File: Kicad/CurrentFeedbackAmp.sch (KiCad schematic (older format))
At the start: 123 parts, among them J1 Test_Etapa_3_Inf, J10 Protecc_Sup_In1, J11 Protecc_Inf_In1, J12 Protecc_Sup_In2, J13 Test_Etapa_3_Inf, J14 Entrada, J15 Salida masa2, J16 Salida tierra, J17 Salida senal, J2 Test_Realim_Out, J3 Salida masa1, J4 Protecc_Sup_Out, J5 Protecc_Inf_Out, J6 Conector Vcc, J7 Conector Vdd, J8 Test_Etapa_3_Inf, J9 Test_Etapa_3_Sup, Q1 TIP42C, Q10 BC559, Q11 BC549, Q12 BC559, Q13 BC559, Q14 BC559, Q15 BC559, Q16 BC549, Q17 BC549, Q18 BC549, Q19 BC559, Q2 BD135, Q20 BC549, Q21 BC559, Q22 BC549, Q23 BC549, Q24 BD136, Q25 BC559, Q26 BC549, Q27 BC549, Q28 BC549, Q29 BC559, Q3 BD136, Q30 BC559, Q31 BC549, Q32 BC559, Q33 BD135, Q34 TIP41C, Q35 BC858, Q36 BC848, Q37 BC848, Q38 BC848, Q4 BC549, Q40 BC858, Q41 BC858, Q5 BC549, Q6 BC559, Q7 BC559, Q8 BC549, Q9 BC559, U1 LM7812_TO220, U2 TL082, U3 LM7912_TO220, U4 LM7805_TO220, U5 LM7905_TO220

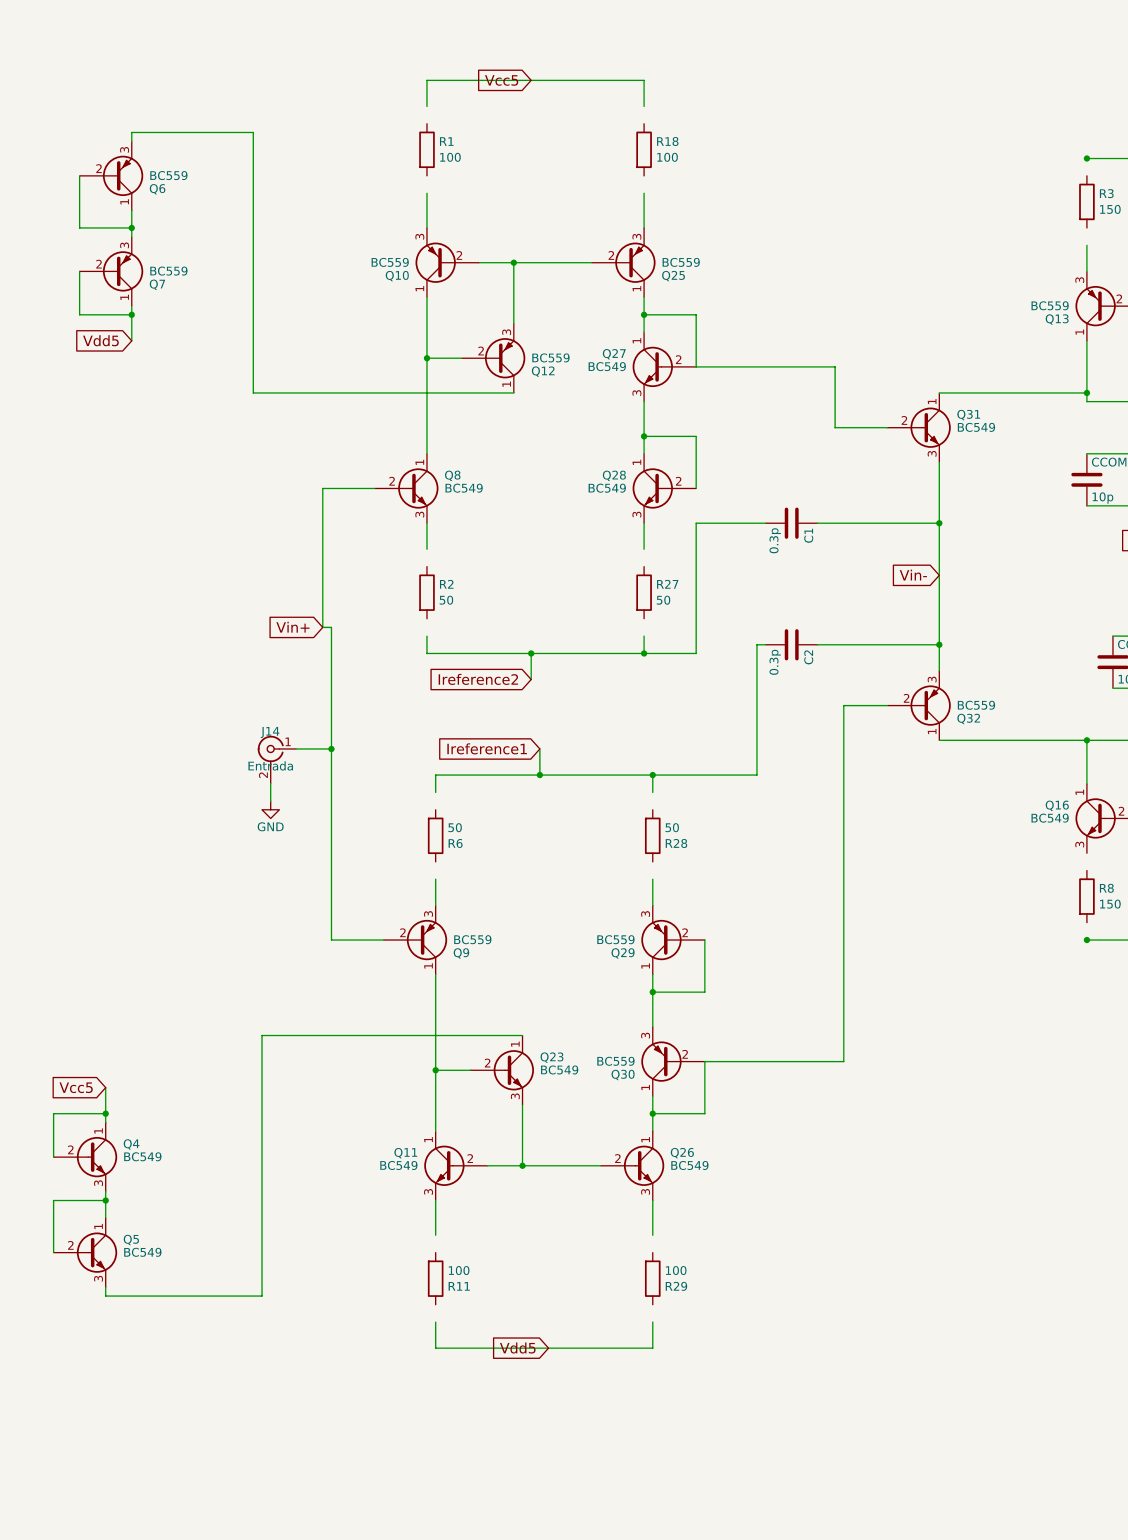
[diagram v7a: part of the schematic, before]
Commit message: Cambios en transitores de etapa siguiente a la fuente de corriente por SMD
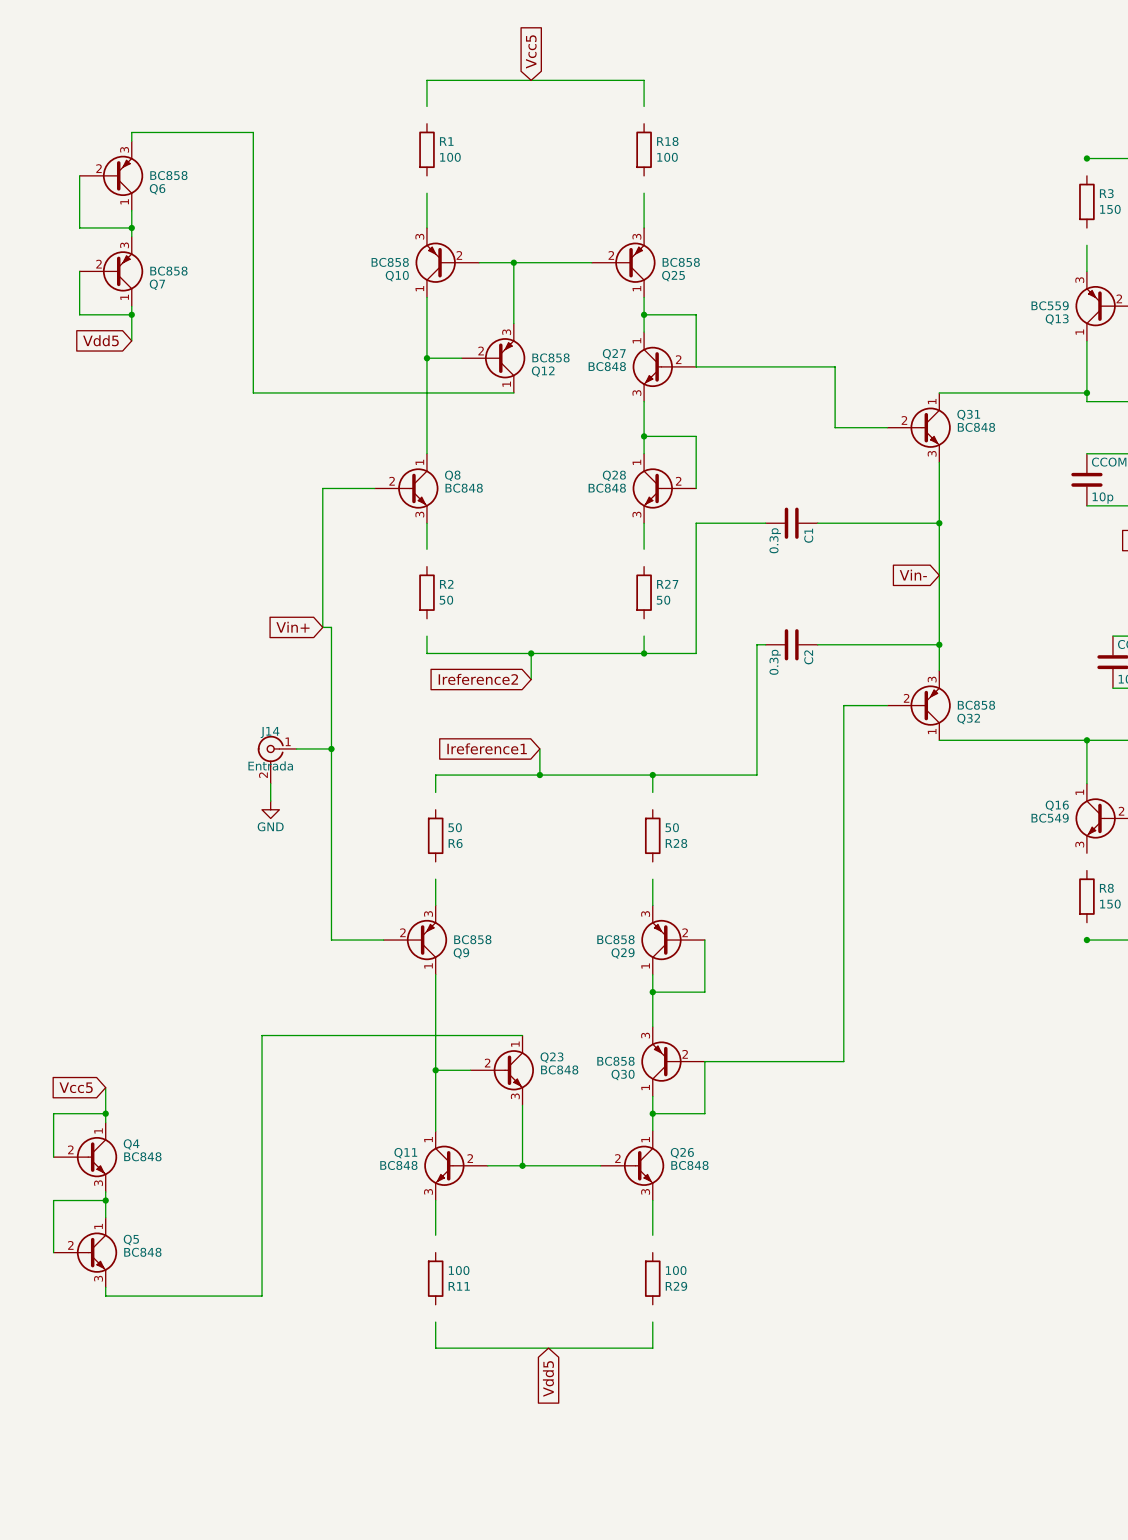
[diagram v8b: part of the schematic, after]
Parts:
- Q10, Q12, Q25, Q29, Q30, Q32, Q6, Q7, Q9: value BC559 -> BC858
- Q11, Q23, Q26, Q27, Q28, Q31, Q4, Q5, Q8: value BC549 -> BC848
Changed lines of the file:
@@
 P 10450 1850
 F 0 "Q10" H 10650 1925 50  0000 L CNN
-F 1 "BC559" H 10650 1850 50  0000 L CNN
+F 1 "BC858" H 10650 1850 50  0000 L CNN
 F 2 "TO_SOT_Packages_THT:TO-92_Inline_Narrow_Oval" H 10650 1775 50  0001 L CIN
 F 3 "" H 10450 1850 50  0001 L CNN
@@
 P 11500 1850
 F 0 "Q25" H 11700 1925 50  0000 L CNN
-F 1 "BC559" H 11700 1850 50  0000 L CNN
+F 1 "BC858" H 11700 1850 50  0000 L CNN
 F 2 "TO_SOT_Packages_THT:TO-92_Inline_Narrow_Oval" H 11700 1775 50  0001 L CIN
 F 3 "" H 11500 1850 50  0001 L CNN
@@
 P 10750 2400
 F 0 "Q12" H 10950 2475 50  0000 L CNN
-F 1 "BC559" H 10950 2400 50  0000 L CNN
+F 1 "BC858" H 10950 2400 50  0000 L CNN
 F 2 "TO_SOT_Packages_THT:TO-92_Inline_Narrow_Oval" H 10950 2325 50  0001 L CIN
 F 3 "" H 10750 2400 50  0001 L CNN
@@
 P 8550 1350
 F 0 "Q6" H 8750 1425 50  0000 L CNN
-F 1 "BC559" H 8750 1350 50  0000 L CNN
+F 1 "BC858" H 8750 1350 50  0000 L CNN
 F 2 "TO_SOT_Packages_THT:TO-92_Inline_Narrow_Oval" H 8750 1275 50  0001 L CIN
 F 3 "" H 8550 1350 50  0001 L CNN
@@
 P 8550 1900
 F 0 "Q7" H 8750 1975 50  0000 L CNN
-F 1 "BC559" H 8750 1900 50  0000 L CNN
+F 1 "BC858" H 8750 1900 50  0000 L CNN
 F 2 "TO_SOT_Packages_THT:TO-92_Inline_Narrow_Oval" H 8750 1825 50  0001 L CIN
 F 3 "" H 8550 1900 50  0001 L CNN
@@
 P 11700 2450
 F 0 "Q27" H 11900 2525 50  0000 L CNN
-F 1 "BC549" H 11900 2450 50  0000 L CNN
+F 1 "BC848" H 11900 2450 50  0000 L CNN
 F 2 "TO_SOT_Packages_THT:TO-92_Inline_Narrow_Oval" H 11900 2375 50  0001 L CIN
 F 3 "" H 11700 2450 50  0001 L CNN
@@
 P 11700 3150
 F 0 "Q28" H 11900 3225 50  0000 L CNN
-F 1 "BC549" H 11900 3150 50  0000 L CNN
+F 1 "BC848" H 11900 3150 50  0000 L CNN
 F 2 "TO_SOT_Packages_THT:TO-92_Inline_Narrow_Oval" H 11900 3075 50  0001 L CIN
 F 3 "" H 11700 3150 50  0001 L CNN
@@
 P 10250 3150
 F 0 "Q8" H 10450 3225 50  0000 L CNN
-F 1 "BC549" H 10450 3150 50  0000 L CNN
+F 1 "BC848" H 10450 3150 50  0000 L CNN
 F 2 "TO_SOT_Packages_THT:TO-92_Inline_Narrow_Oval" H 10450 3075 50  0001 L CIN
 F 3 "" H 10250 3150 50  0001 L CNN
@@
 P 13200 2800
 F 0 "Q31" H 13400 2875 50  0000 L CNN
-F 1 "BC549" H 13400 2800 50  0000 L CNN
+F 1 "BC848" H 13400 2800 50  0000 L CNN
 F 2 "TO_SOT_Packages_THT:TO-92_Inline_Narrow_Oval" H 13400 2725 50  0001 L CIN
 F 3 "" H 13200 2800 50  0001 L CNN
@@
 P 10300 5750
 F 0 "Q9" H 10500 5825 50  0000 L CNN
-F 1 "BC559" H 10500 5750 50  0000 L CNN
+F 1 "BC858" H 10500 5750 50  0000 L CNN
 F 2 "TO_SOT_Packages_THT:TO-92_Inline_Narrow_Oval" H 10500 5675 50  0001 L CIN
 F 3 "" H 10300 5750 50  0001 L CNN
@@
 P 10800 6500
 F 0 "Q23" H 11000 6575 50  0000 L CNN
-F 1 "BC549" H 11000 6500 50  0000 L CNN
+F 1 "BC848" H 11000 6500 50  0000 L CNN
 F 2 "TO_SOT_Packages_THT:TO-92_Inline_Narrow_Oval" H 11000 6425 50  0001 L CIN
 F 3 "" H 10800 6500 50  0001 L CNN
@@
 P 10500 7050
 F 0 "Q11" H 10700 7125 50  0000 L CNN
-F 1 "BC549" H 10700 7050 50  0000 L CNN
+F 1 "BC848" H 10700 7050 50  0000 L CNN
 F 2 "TO_SOT_Packages_THT:TO-92_Inline_Narrow_Oval" H 10700 6975 50  0001 L CIN
 F 3 "" H 10500 7050 50  0001 L CNN
@@
 P 11750 5750
 F 0 "Q29" H 11950 5825 50  0000 L CNN
-F 1 "BC559" H 11950 5750 50  0000 L CNN
+F 1 "BC858" H 11950 5750 50  0000 L CNN
 F 2 "TO_SOT_Packages_THT:TO-92_Inline_Narrow_Oval" H 11950 5675 50  0001 L CIN
 F 3 "" H 11750 5750 50  0001 L CNN
@@
 P 11750 6450
 F 0 "Q30" H 11950 6525 50  0000 L CNN
-F 1 "BC559" H 11950 6450 50  0000 L CNN
+F 1 "BC858" H 11950 6450 50  0000 L CNN
 F 2 "TO_SOT_Packages_THT:TO-92_Inline_Narrow_Oval" H 11950 6375 50  0001 L CIN
 F 3 "" H 11750 6450 50  0001 L CNN
@@
 P 8400 7550
 F 0 "Q5" H 8600 7625 50  0000 L CNN
-F 1 "BC549" H 8600 7550 50  0000 L CNN
+F 1 "BC848" H 8600 7550 50  0000 L CNN
 F 2 "TO_SOT_Packages_THT:TO-92_Inline_Narrow_Oval" H 8600 7475 50  0001 L CIN
 F 3 "" H 8400 7550 50  0001 L CNN
@@
 P 13200 4400
 F 0 "Q32" H 13400 4475 50  0000 L CNN
-F 1 "BC559" H 13400 4400 50  0000 L CNN
+F 1 "BC858" H 13400 4400 50  0000 L CNN
 F 2 "TO_SOT_Packages_THT:TO-92_Inline_Narrow_Oval" H 13400 4325 50  0001 L CIN
 F 3 "" H 13200 4400 50  0001 L CNN
@@
 P 11550 7050
 F 0 "Q26" H 11750 7125 50  0000 L CNN
-F 1 "BC549" H 11750 7050 50  0000 L CNN
+F 1 "BC848" H 11750 7050 50  0000 L CNN
 F 2 "TO_SOT_Packages_THT:TO-92_Inline_Narrow_Oval" H 11750 6975 50  0001 L CIN
 F 3 "" H 11550 7050 50  0001 L CNN
@@
 P 8400 7000
 F 0 "Q4" H 8600 7075 50  0000 L CNN
-F 1 "BC549" H 8600 7000 50  0000 L CNN
+F 1 "BC848" H 8600 7000 50  0000 L CNN
 F 2 "TO_SOT_Packages_THT:TO-92_Inline_Narrow_Oval" H 8600 6925 50  0001 L CIN
 F 3 "" H 8400 7000 50  0001 L CNN
@@
 Wire Wire Line
 	8650 1100 9350 1100
-Text GLabel 10950 800  0    60   Input ~ 0
+Text GLabel 10950 800  1    60   Input ~ 0
 Vcc5
-Text GLabel 11050 8100 0    60   Input ~ 0
+Text GLabel 11050 8100 3    60   Input ~ 0
 Vdd5
 Wire Wire Line
